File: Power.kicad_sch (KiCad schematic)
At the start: 25 parts, among them Q5 IRLML2803, Q6 SiRA99DP, U2 TPS259621DDA, U4 ADM1176-1ARMZ-R7

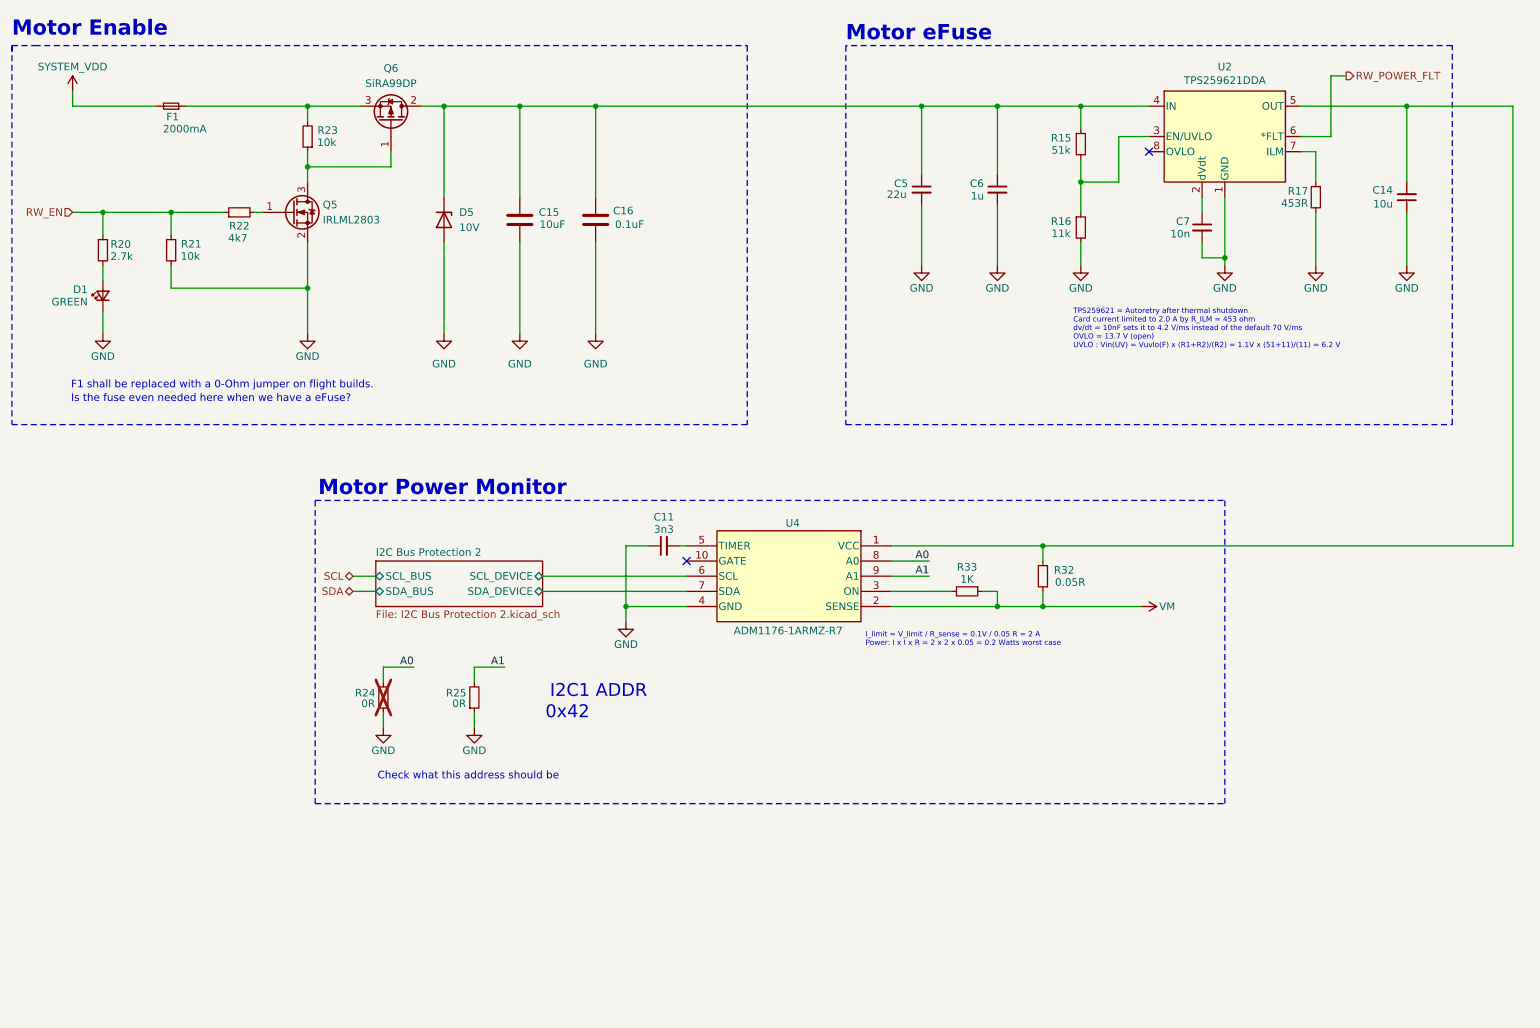
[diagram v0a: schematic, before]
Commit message: Checked all power and voltage ratings and corrected where needed. Still need footprints and layout completed.
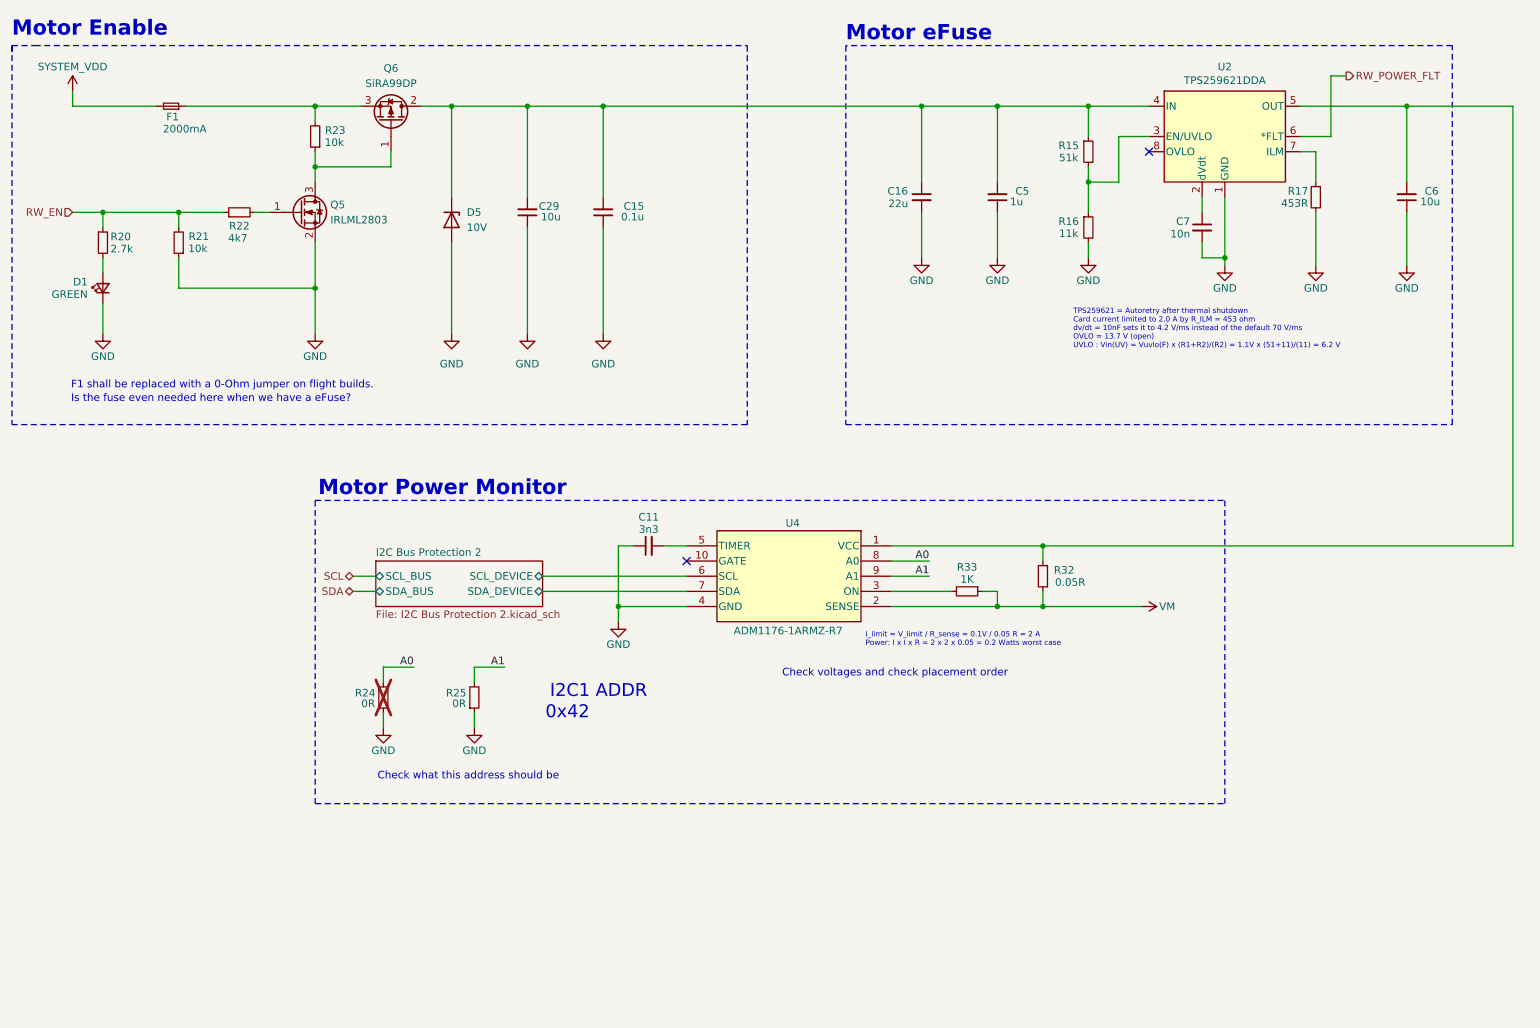
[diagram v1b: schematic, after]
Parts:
- removed C14: 10u, Capacitor_SMD:C_0805_2012Metric, symbol Device:C_Small
- removed C15: 10uF, Capacitor_SMD:C_1210_3225Metric, symbol Device:C
- removed C16: 0.1uF, Capacitor_SMD:C_0603_1608Metric, symbol Device:C
- added C15: 0.1u, Capacitor_SMD:C_0402_1005Metric_Pad0.74x0.62mm_HandSolder, symbol Device:C_Small
- added C16: 22u, Capacitor_SMD:C_1210_3225Metric_Pad1.33x2.70mm_HandSolder, symbol Device:C_Small
- added C29: 10u, Capacitor_SMD:C_1206_3216Metric_Pad1.33x1.80mm_HandSolder, symbol Device:C_Small
- C5: value 22u -> 1u; footprint Capacitor_SMD:C_1210_3225Metric -> Capacitor_SMD:C_0603_1608Metric; DPN 587-3473-1-ND -> (none); DST Digi-Key -> (none); Digikey (none) -> https://www.digikey.com/en/products/detail/samsung-electro-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; MFR Taiyo Yuden -> (none); MPN TMK107BJ105KAHT -> (none); Part (none) -> CL10B105KA8NNNC
- C6: value 1u -> 10u; footprint Capacitor_SMD:C_0603_1608Metric -> Capacitor_SMD:C_1206_3216Metric_Pad1.33x1.80mm_HandSolder; DPN 490-GCM32EC71E226KE36KCT-ND -> (none); DST Digi-Key -> (none); Digikey (none) -> https://www.digikey.com/en/products/detail/samsung-electro-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; MFR Murata Electronics -> (none); MPN GCM32EC71E226KE36K -> (none); Part (none) -> CL31B106KAHNNNE
- F1: Digikey (none) -> https://www.digikey.com/en/products/detail/panasonic-electr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; Part (none) -> ERB-RE2R00V
- R32: footprint Resistor_SMD:R_2512_6332Metric -> Resistor_SMD:R_0805_2012Metric_Pad1.20x1.40mm_HandSolder; Digikey (none) -> https://www.digikey.com/en/products/detail/panasonic-electr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; Part (none) -> ERJ-L06KF50MV
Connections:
- net GND: now also C5.1, C6.1, C15.1, C16.2, C29.1; no longer C5.2, C6.2
- net at D5.1 (K), Q6.2 (D), R15.1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: now also C5.2, C15.2, C16.1, C29.2; no longer C5.1, C6.1
- net at R32.2, U2.5 (OUT), U4.1 (VCC): now also C6.2
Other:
- note added: "Check voltages and check placement order"
- moved on the sheet: C11, D1, D5, Q5, R15, R16, R20, R21, R23

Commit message: Clean notes
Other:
- note removed: "Check voltages and check placement order"
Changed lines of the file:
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@@
-		)
-	)
-	(text "Check voltages and check placement order"
-		(exclude_from_sim no)
-		(at 154.432 131.318 0)
-		(effects
-			(font
-				(size 1.27 1.27)
-				(color 255 0 0 1)
-			)
-			(justify left bottom)
 		)
 	)

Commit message: Add more test points
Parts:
- added TP2, TP3, TP4: ~, symbol Argus_RW_Library:5001
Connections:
- net SWITCHED_POWER: now reaches C15.2, C16.1, C29.2, C5.2, D5.1 (K), Q6.2 (D), R15.1, U2.4 (IN)
- net SWITCHED_POWER: now also TP3.TP
- net FUSED_POWER: now reaches F1.1, Q6.3 (S), R23.2
- net FUSED_POWER: now also TP2.TP
- net eFUSED_POWER: now reaches C6.2, R32.2, U2.5 (OUT), U4.1 (VCC)
- net eFUSED_POWER: now also TP4.TP

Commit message: Layout mostly complete
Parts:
- removed C29: 10u, Capacitor_SMD:C_1206_3216Metric_Pad1.33x1.80mm_HandSolder, symbol Device:C_Small
- added L1: 1UH, Argus_RW_Library:HCM1A1104V2, symbol Argus_RW_Library:HCM1A1104V2
- added R52, R53: 0R, Resistor_SMD:R_2512_6332Metric_Pad1.40x3.35mm_HandSolder, symbol Device:R_Small
- added R56, R57: 0R, Resistor_SMD:R_0402_1005Metric_Pad0.72x0.64mm_HandSolder, symbol Device:R_Small
- F1: value 2000mA -> 3000mA
- R24: footprint Resistor_SMD:R_0603_1608Metric -> Resistor_SMD:R_0402_1005Metric_Pad0.72x0.64mm_HandSolder
- R25: footprint Resistor_SMD:R_0603_1608Metric -> Resistor_SMD:R_0402_1005Metric_Pad0.72x0.64mm_HandSolder; now not fitted
- R32: value 0.05R -> 0.01R; Digikey https://www.digikey.com/en/products/detail/panasonic-electronic-components/ERJ-L06KF50MV/966111 -> https://www.digikey.com/en/products/detail/panasonic-electronic-components/ERJ-8BWFR010V/1711632; Part ERJ-L06KF50MV -> ERJ-8BWFR010V
- TP2, TP3, TP4: footprint (none) -> Argus_RW_Library:KEYSTONE_5001
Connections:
- net A0: now also R25.2
- net A1: now also R56.2, R57.2; no longer R25.2
- net FUSED_POWER: now also R53.1
- net GND: now also R57.1; no longer R24.1
- net SWITCHED_POWER: now also R52.2
- net VM: now also L1.2; no longer R32.1, R33.1, U4.2 (SENSE)
- net eFUSED_POWER: now also R24.1, R52.1, R56.1
- net SYSTEM_VDD renamed VMAIN
- net VMAIN: now also R53.2
- new net MON_POWER: L1.1, R32.1, R33.1, U4.2 (SENSE)
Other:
- note added: "0x??"
- note added: "Bypasses for the fuses"
- note added: "Fuse Bypass Jumpers"
- note added: "I_limit = V_limit / R_sense = 0.1V / 0.01 R = 10 A Power: I x I x R = 10 x 10 x 0.01 = 1 Watts worst case"
- note added: "Not sure of how to configure this"
- note added: "PI Filter"
- note added: "Should be 0x46"
- note removed: "0x42"
- note removed: "Check what this address should be"
- note removed: "I_limit = V_limit / R_sense = 0.1V / 0.05 R = 2 A Power: I x I x R = 2 x 2 x 0.05 = 0.2 Watts worst case"
- note removed: "Is the fuse even needed here when we have a eFuse?"
- title: (none) -> Argus Reaction Wheel
- moved on the sheet: C11, R32, R33, U4

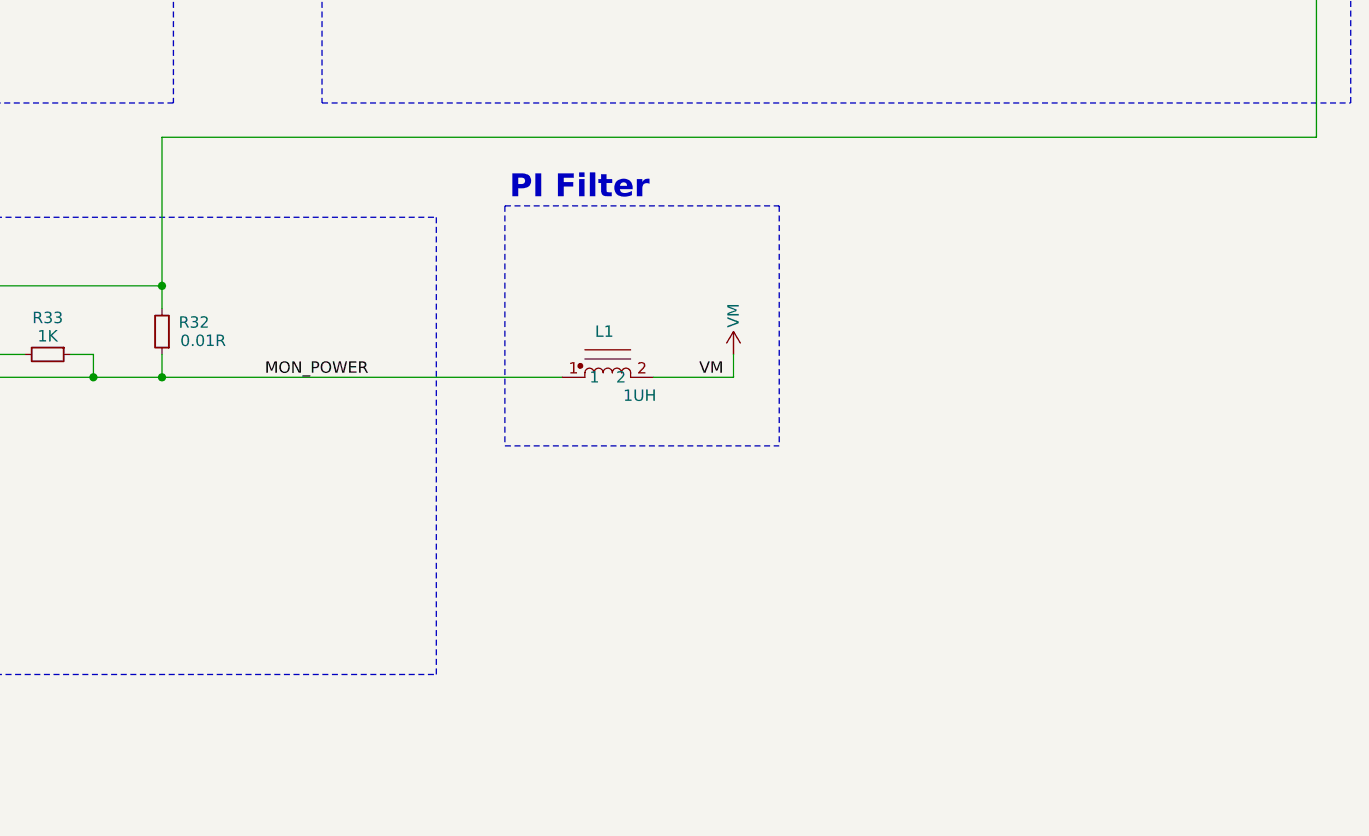
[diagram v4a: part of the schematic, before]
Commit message: Push requested changes - silkscreen, copper width, pi filter
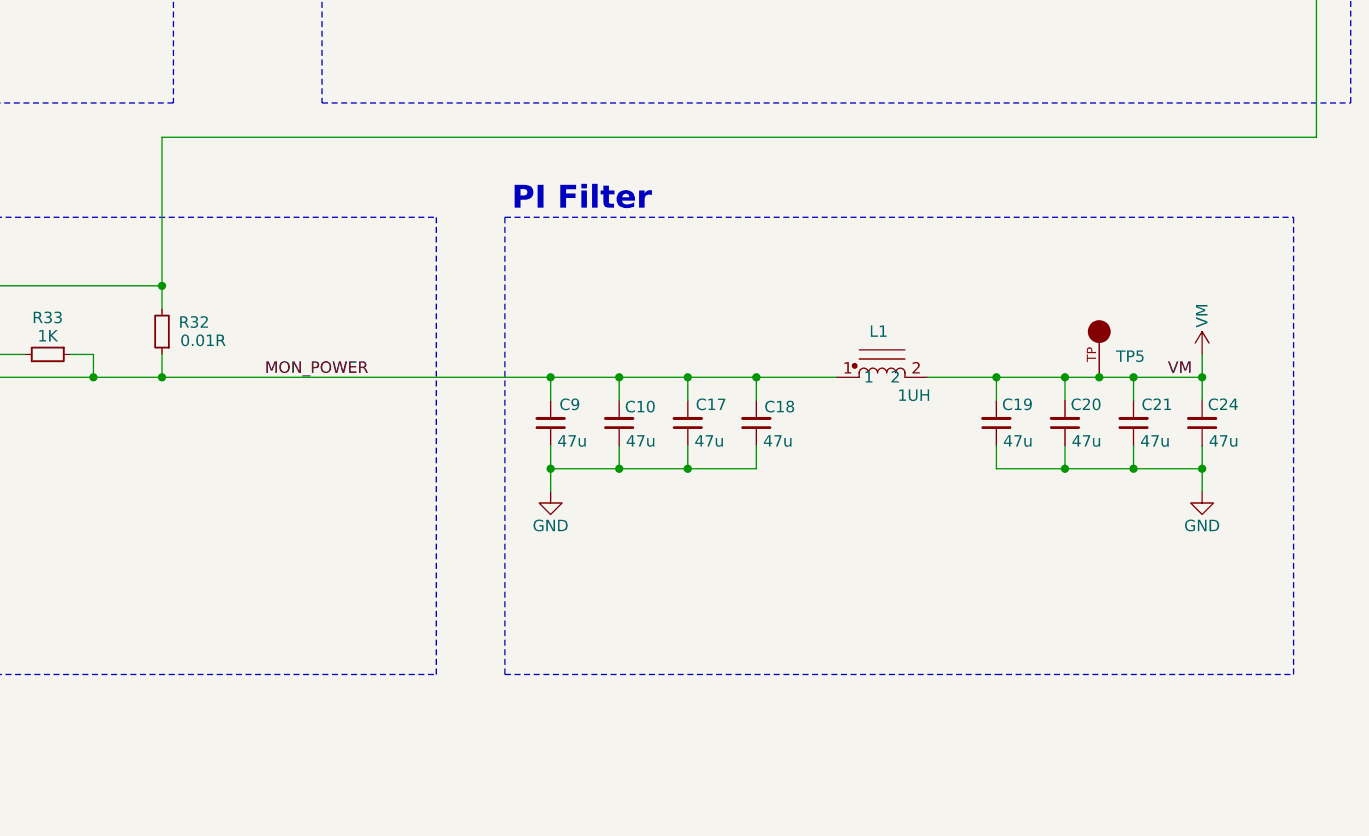
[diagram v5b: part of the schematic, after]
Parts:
- added C10, C17, C18, C19, C20, C21, C24, C9: 47u, Capacitor_SMD:C_1206_3216Metric_Pad1.33x1.80mm_HandSolder, symbol Device:C_Small
- added TP5: ~, Argus_RW_Library:KEYSTONE_5001, symbol Argus_RW_Library:5001
- F1: Digikey https://www.digikey.com/en/products/detail/panasonic-electr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 -> https://www.digikey.com/en/products/detail/bourns-inc/SF-06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; Part ERB-RE2R00V -> SF-0603S300-2
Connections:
- net GND: now also C10.1, C17.1, C18.1, C19.1, C20.1, C21.1, C24.1, C9.1
- net MON_POWER: now also C10.2, C17.2, C18.2, C9.2
- net VM: now also C19.2, C20.2, C21.2, C24.2, TP5.TP
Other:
- moved on the sheet: L1

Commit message: Add and correct BOM for easy Digikey ordering
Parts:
- C10, C17, C18, C19, C20, C21, C24, C9: Digikey PN (none) -> 445-8047-1-ND; MPN (none) -> C3216X5R1E476M160AC
- C11: value 3n3 -> 3.3n; Digikey (none) -> https://www.digikey.com/en/products/detail/kemet/C0603C332K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; Digikey PN (none) -> 399-C0603C332K4REC7411CT-ND; MPN (none) -> C0603C332K4REC7411; Part (none) -> C0603C332K4REC7411
- C15: value 0.1u -> 100n; Digikey https://www.digikey.com/en/products/detail/samsung-electro-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 -> https://www.digikey.com/en/products/detail/kemet/C0402C103K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; Digikey PN (none) -> 399-C0402C103K3RACTUCT-ND; MPN (none) -> C0402C103K3RACTU; Part CL05B104KA5NNNC -> C0402C103K3RACTU
- C16: Digikey (none) -> https://www.digikey.com/en/products/detail/murata-electroni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; Digikey PN (none) -> 490-GCM32EC71E226KE36KCT-ND; Part (none) -> GCM32EC71E226KE36K
- C5: Digikey PN (none) -> 1276-1184-1-ND; MPN (none) -> CL10B105KA8NNNC
- C6: Digikey PN (none) -> 1276-1804-1-ND; MPN (none) -> CL31B106KAHNNNE
- C7: Digikey (none) -> https://www.digikey.com/en/products/detail/samsung-electro-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; Digikey PN (none) -> 490-4934-1-ND; MPN C0603C103J3GECAUTO -> CL10B103KO8WPNC; Part (none) -> CL10B103KO8WPNC
- D1: value GREEN -> GREEN LED; Digikey (none) -> https://www.digikey.com/en/products/detail/inolux/IN-S63AT5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; Digikey PN (none) -> 1830-1064-1-ND; Part (none) -> IN-S63AT5A
- D5: Digikey (none) -> https://www.digikey.com/en/products/detail/nexperia-usa-inc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; Digikey PN (none) -> 1727-2744-1-ND; MPN (none) -> PTVS10VZ1USKYL; Part (none) -> PTVS10VZ1USKYL
- F1: Digikey PN (none) -> SF-0603S300-2CT-ND; MPN (none) -> SF-0603S300-2
- L1: Digikey PN (none) -> 283-HCM1A1104V2-1R0-RCT-ND; MPN (none) -> HCM1A1104V2-1R0-R
- Q5: Digikey (none) -> https://www.digikey.com/en/products/detail/infineon-technol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; Digikey PN (none) -> IRLML2803PBFCT-ND; MPN (none) -> IRLML2803TRPBF; Part (none) -> IRLML2803TRPBF
- Q6: Digikey (none) -> https://www.digikey.com/en/products/detail/vishay-siliconix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; Digikey PN (none) -> SIRA99DP-T1-GE3CT-ND; MPN (none) -> SIRA99DP-T1-GE3; Part (none) -> SIRA99DP-T1-GE3
- R15: Digikey (none) -> https://www.digikey.com/en/products/detail/yageo/RC0603FR-0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; Digikey PN (none) -> 311-51.0KHRCT-ND; MPN RMCF0603FT10K0 -> RC0603FR-0751KL; Part (none) -> RC0603FR-0751KL
- R16: Digikey (none) -> https://www.digikey.com/en/products/detail/yageo/RC0603FR-0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; Digikey PN (none) -> 311-11.0KHRCT-ND; MPN RMCF0603FT10K0 -> RC0603FR-0711KL; Part (none) -> RC0603FR-0711KL
- R17: Digikey (none) -> https://www.digikey.com/en/products/detail/yageo/RC0603FR-0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; Digikey PN (none) -> 311-453HRCT-ND; MPN RMCF0603FT604R -> RC0603FR-07453RL; Part (none) -> RC0603FR-07453RL
- R20: Digikey (none) -> https://www.digikey.com/en/products/detail/te-connectivity-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; Digikey PN (none) -> A129693CT-ND; Part (none) -> CRGCQ0603F2K7
- R21, R23: Digikey (none) -> https://www.digikey.com/en/products/detail/yageo/RC0603FR-0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; Digikey PN (none) -> 311-10.0KHRCT-ND; Part (none) -> RC0603FR-0710KL
- R22: Digikey (none) -> https://www.digikey.com/en/products/detail/yageo/RC0603FR-0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; Digikey PN (none) -> 311-4.70KHRCT-ND; MPN (none) -> RC0603FR-074K7L; Part (none) -> RC0603FR-074K7L
- R24, R25, R56, R57: Digikey (none) -> https://www.digikey.com/en/products/detail/yageo/RC0402JR-0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; Digikey PN (none) -> 311-0.0JRCT-ND; MPN (none) -> RC0402JR-070RL; Part (none) -> RC0402JR-070RL
- R32: Digikey PN (none) -> P.010AUCT-ND; MPN (none) -> ERJ-8BWFR010V
- R33: value 1K -> 1k; Digikey (none) -> https://www.digikey.com/en/products/detail/yageo/RC0603FR-0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; Digikey PN (none) -> 311-1.00KHRCT-ND; MPN (none) -> RC0603FR-071KL; Part (none) -> RC0603FR-071KL
- R52, R53: Digikey https://www.digikey.com/en/products/detail/vishay-dale/CRCW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 -> https://www.digikey.com/en/products/detail/yageo/RC2512FK-0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; Digikey PN (none) -> 13-RC2512FK-070RLCT-ND; MPN (none) -> RC2512FK-070RL; Part CRCW251222R0FKEGHP -> RC2512FK-070RL
- TP2, TP3, TP4, TP5: value ~ -> TP; Digikey (none) -> https://www.digikey.com/en/products/detail/keystone-electro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; Digikey PN (none) -> 36-5001-ND; MPN (none) -> 5001; Part (none) -> 5001
- U2: Digikey (none) -> https://www.digikey.com/en/products/detail/texas-instrument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; Digikey PN (none) -> 296-TPS259621DDARCT-ND; Part (none) -> TPS259620DDAT
- U4: Digikey (none) -> https://www.digikey.com/en/products/detail/analog-devices-i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; Digikey PN (none) -> 505-ADM1176-1ARMZ-R7CT-ND; MPN (none) -> ADM1176-1ARMZ-R7; Part (none) -> ADM1176-1ARMZ-R7
